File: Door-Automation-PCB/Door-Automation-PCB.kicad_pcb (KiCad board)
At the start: 2 copper layers, 70 x 140 mm, 17 parts, among them J1 Conn_01x15_Female, J10 Solenoid conn, J2 Conn_01x15_Female, J3 12V_IN, J5 3.3V, J8 9V, Q1 N-MOSFET, U2 buck_converter, U4 buck_converter

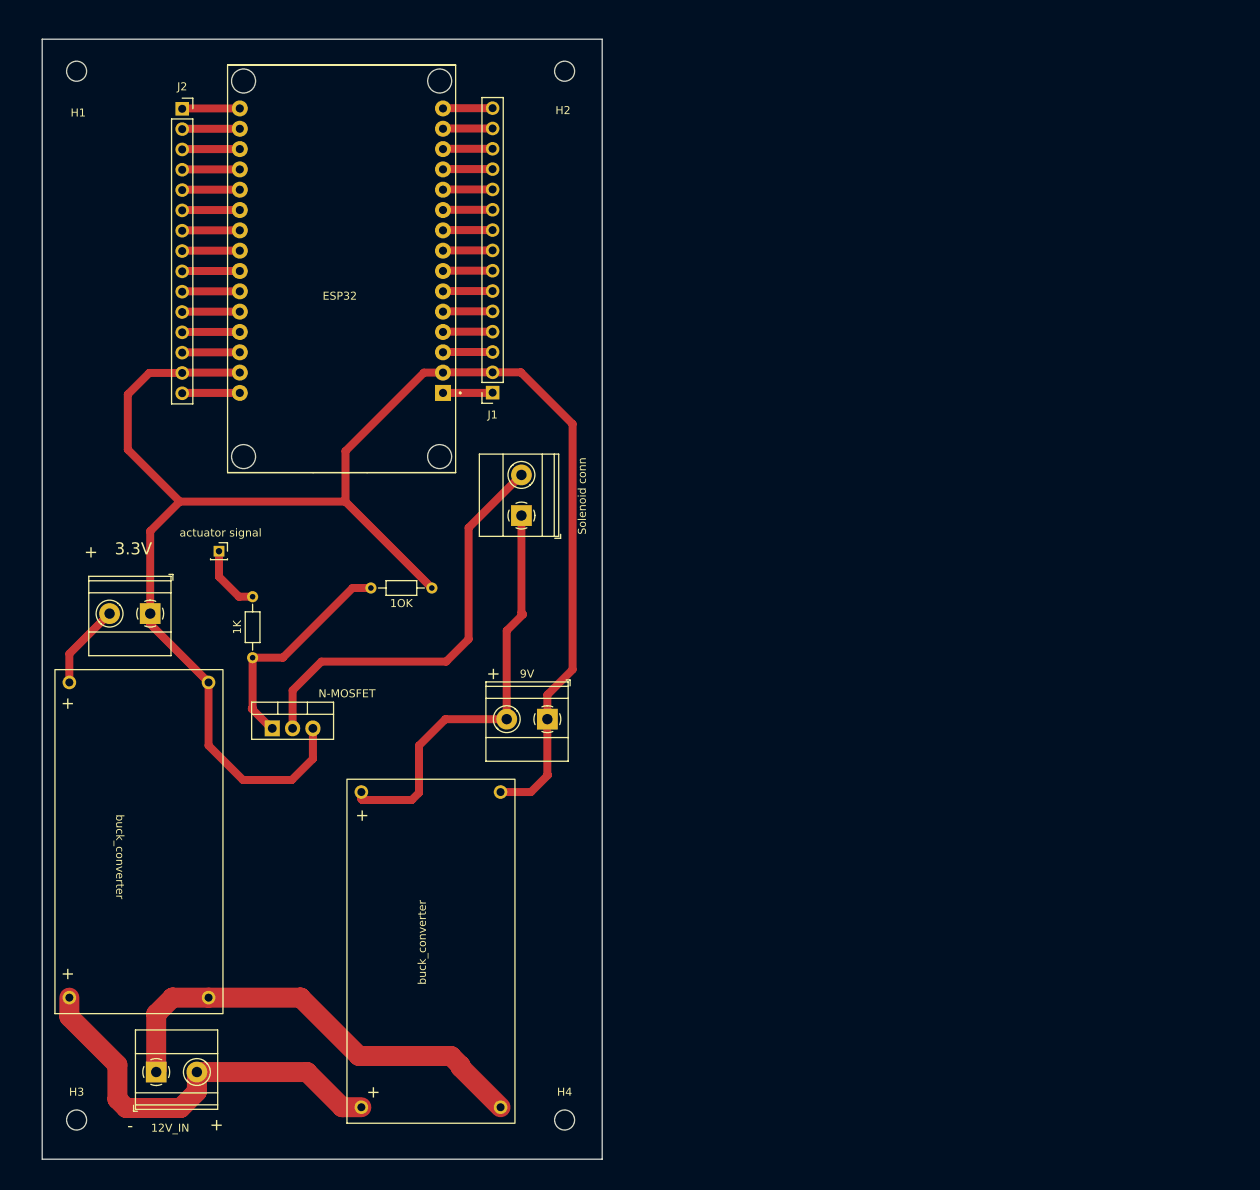
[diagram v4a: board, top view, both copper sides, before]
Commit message: added copper pour
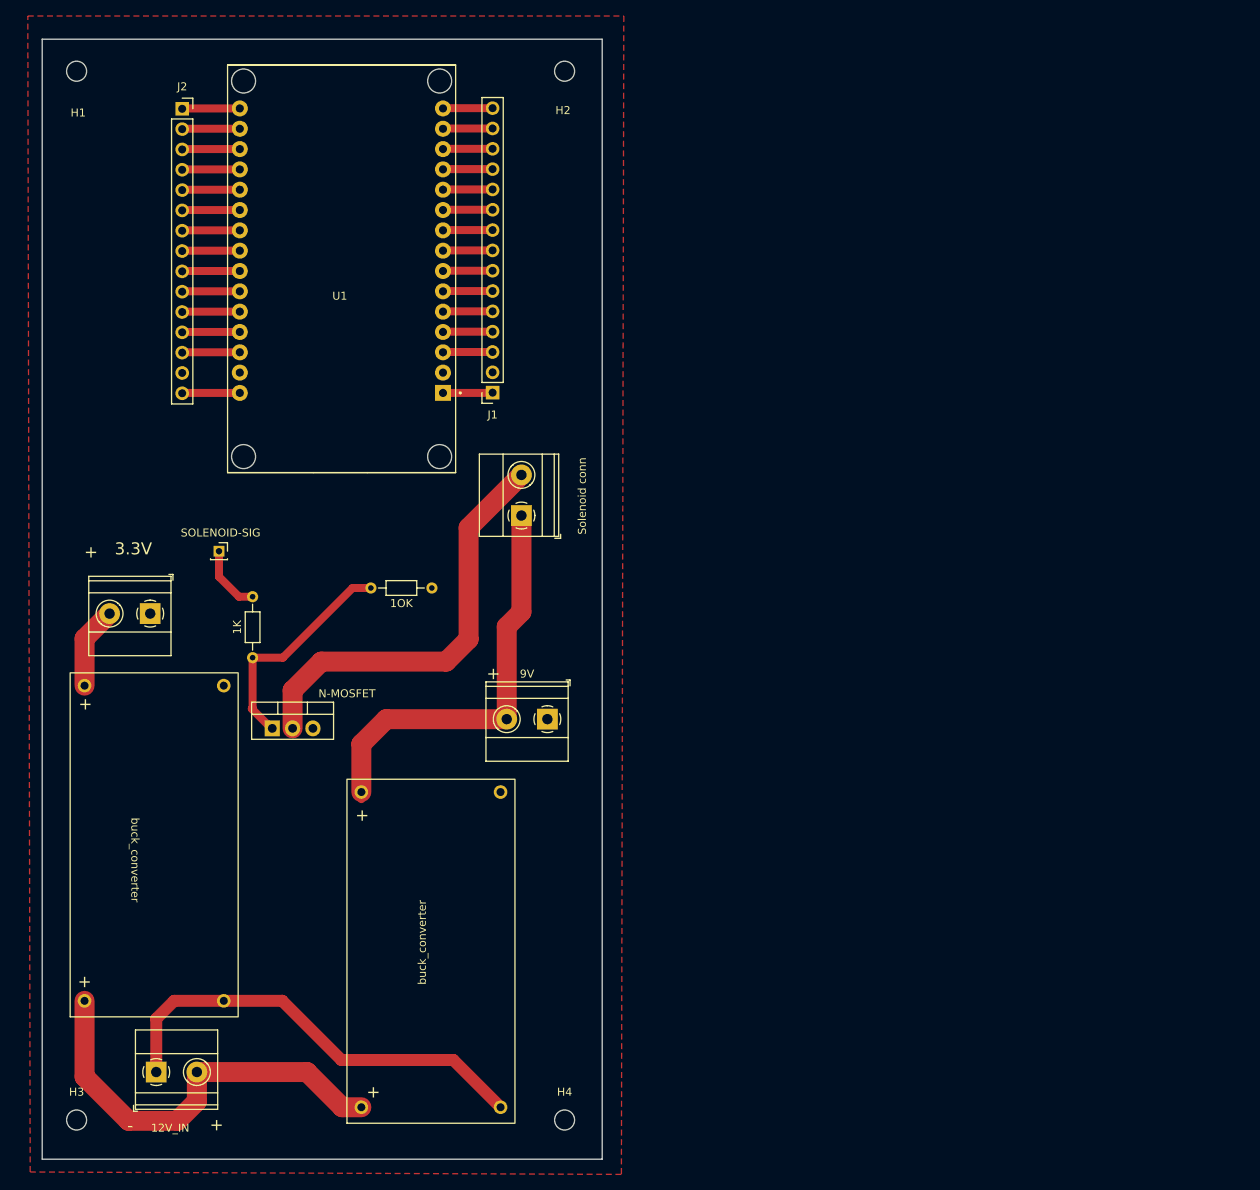
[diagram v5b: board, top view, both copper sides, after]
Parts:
- SOLENOID-SIG: renamed from actuator signal
- moved U2 1.94 mm to (83.5, 162.2)
- renumbered ESP32 to U1
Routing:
- net /GND: track 215.5 -> 0.11 mm
- net Net-(J3-Pad2): track 51.3 -> 52.9 mm
- net Net-(J3-Pad1): track 57.0 -> 56.1 mm
- net /+9V: track 53.1 -> 52.6 mm
- added copper zone on F.Cu, net /GND
